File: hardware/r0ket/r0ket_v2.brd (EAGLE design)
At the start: 127.6 x 60.4 mm, 89 parts, among them IC1 MCP1700, IC2 LPC1343, IC3 AT45DB041D, IC4 NRF24L01SMD, IC5 MCP73833, IC6 TB62737, M0DULA M06X2PTH, M0DULB M06X2PTH, Q1 Q12M-SMD-S, Q2 3.2X2.5CRYSTAL, SW1 JS102011SAQN, T1 SI2301DS, T3 SI2301DS, T4 SI2301DS, T5 SI2301DS, T6 SI2301DS, X1 MICROUSB, X1_ JST-PH3, X2 NOKIA

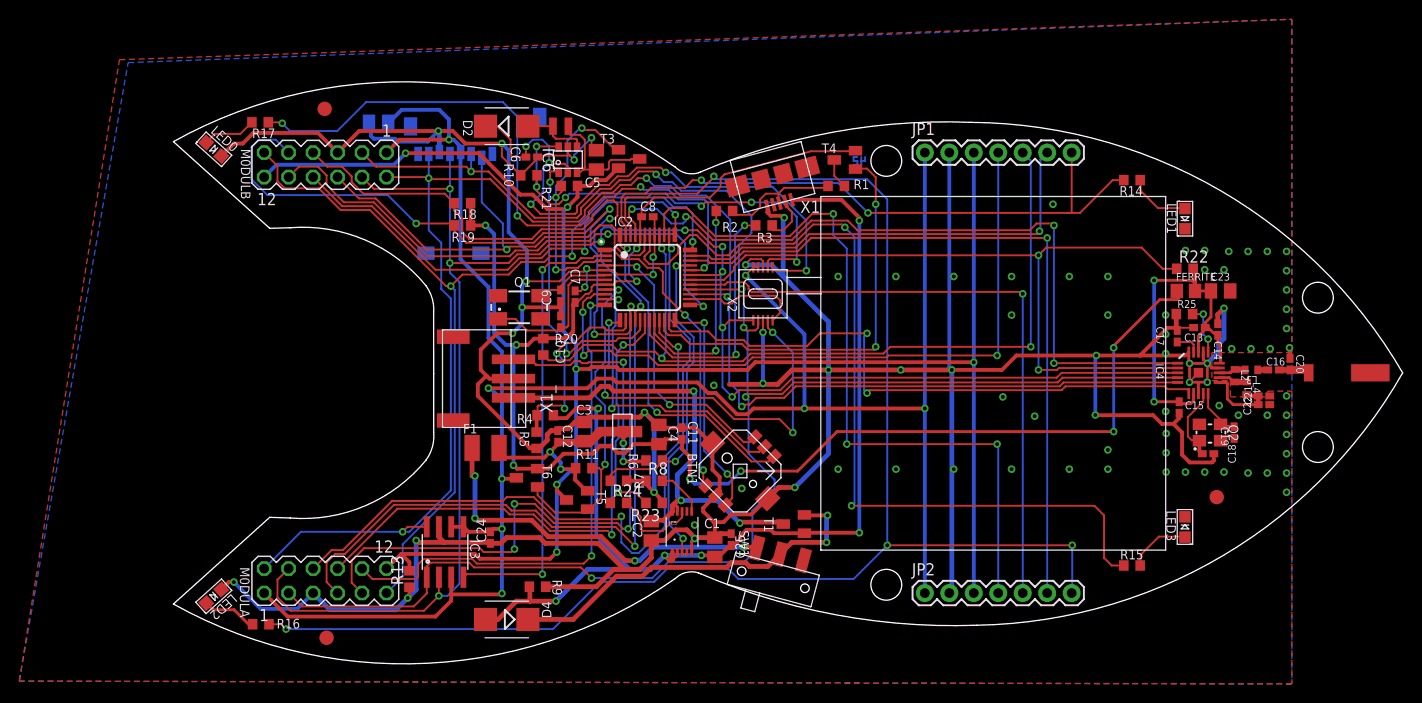
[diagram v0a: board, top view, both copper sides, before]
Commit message: removed a lot of components
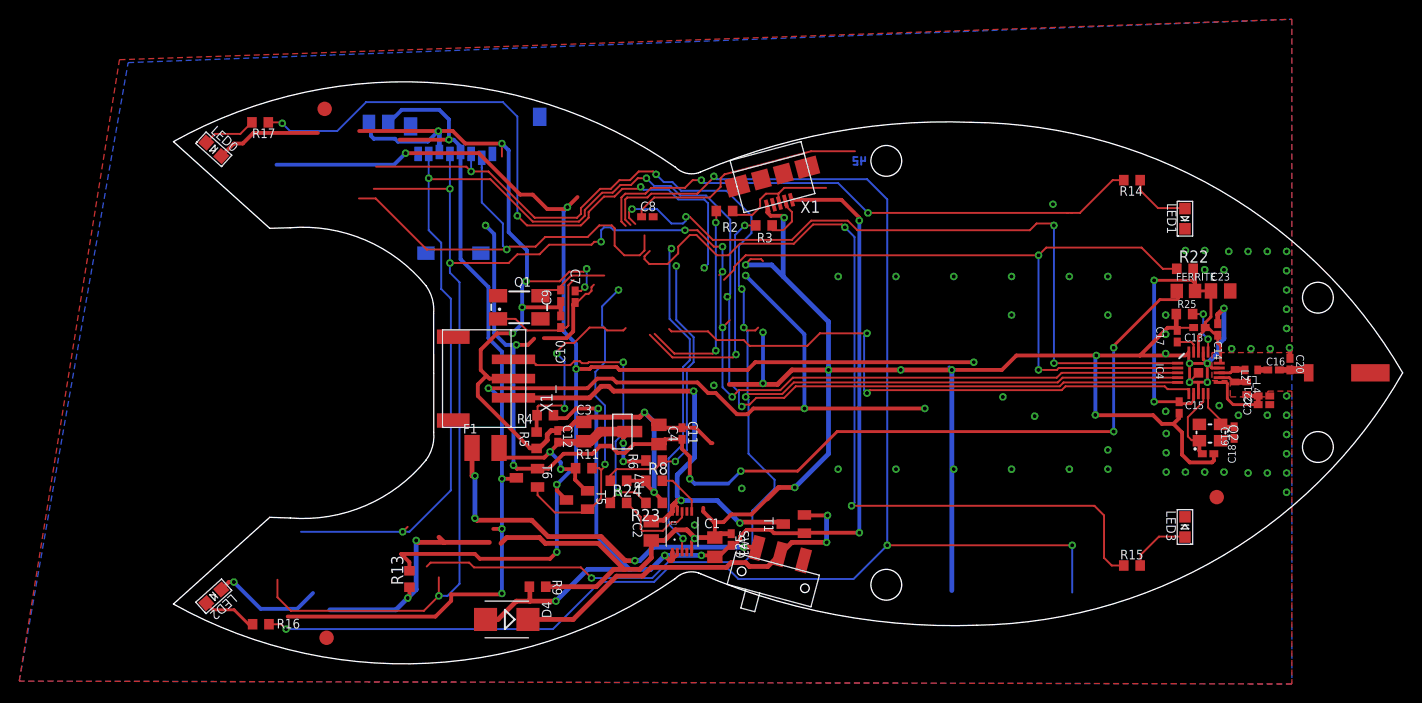
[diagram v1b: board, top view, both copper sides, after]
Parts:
- removed BTN1: MCMT5-F-V, badge:MCMT5-F-V
- removed C24, C6: 100nF, rcl:C0402K
- removed C5: 10uF, rcl:C0805K
- removed D2: SS14, diode:SMB
- removed IC2: LPC1343, microbuilder:LQFP48
- removed IC3: AT45DB041D, SparkFun:SO08
- removed IC6: TB62737, badge:SUPERSOT6
- removed JP1, JP2: (no value), SparkFun:1X07
- removed L1: 4u7, badge:0806
- removed M0DULA, M0DULB: M06X2PTH, con-lstb:MA06-2
- removed R1: 1k5, rcl:R0603
- removed R10: 15, rcl:R0603
- removed R18, R19: 4k7, rcl:R0603
- removed R20: 100k, rcl:R0603
- removed R21: 10k, rcl:R0603
- removed T3, T4: SI2301DS, transistor-small-signal:SOT23
- removed X2: NOKIA, badge:DF23
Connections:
- removed net BTN0: BTN1.3, IC2.4
- removed net BTN1: BTN1.4, IC2.24
- removed net BTN2: BTN1.6, IC2.1
- removed net BTN3: BTN1.1, IC2.48
- removed net BTN4: BTN1.2, IC2.11
- removed net BUSINT: IC2.36, M0DULA.11, M0DULB.11
- removed net CS_DF: IC2.2, IC3.4
- removed net HB0: IC2.39, JP2.4
- removed net HB1: IC2.29, JP2.5
- removed net HB2: IC2.34, JP2.6
- removed net HB3: IC2.10, JP1.4
- removed net HB4: IC2.40, JP1.5, R20.1
- removed net HB5: IC2.35, JP1.6
- removed net LCD_BL: IC2.17, IC6.1
- removed net LCD_BLEN: IC2.3, R21.1, T3.1
- removed net LCD_CS: IC2.13, X2.4
- removed net LCD_RST: IC2.26, X2.5
- removed net LED+: C6.2, D2.C, IC6.2, X2.6
- removed net LED-: IC6.6, R10.2, X2.7
- removed net N$14: D2.A, IC6.4, L1.2
- removed net N$20: R1.1, T4.3
- removed net SCL: IC2.15, M0DULA.9, M0DULB.9, R19.1
- removed net SDA: IC2.16, M0DULA.7, M0DULB.7, R18.2
- removed net SS0: IC2.21, M0DULA.6
- removed net SS1: IC2.18, M0DULA.8
- removed net SS2: IC2.12, M0DULA.10
- removed net SS4: IC2.37, M0DULB.8
- removed net SS5: IC2.25, M0DULB.10
- removed net USB_CONNECT: IC2.22, T4.1
- removed net VCC_LCD: C5.2, IC6.3, L1.1, T3.3
- net +3V3: no longer IC2.44, IC2.8, R18.1, R19.2, R20.2, T4.2
- net +3V3_EXP: no longer C24.2, IC3.3, IC3.5, IC3.6, JP1.1, JP2.1, M0DULA.1, M0DULB.1, X2.10, X2.9
- net CE: no longer IC2.45
- net CHRG_STAT: no longer IC2.38
- net CSN: no longer IC2.30
- net D+: no longer R1.2
- net GND: no longer BTN1.5, BTN1.TAB1, BTN1.TAB2, C24.1, C5.1, C6.1, IC2.41, IC2.5, IC3.7, IC6.5, JP1.2, JP2.2, M0DULA.5, M0DULB.5, R10.1, X2.3, X2.8
- net IRQ: no longer IC2.23
- net LED0: no longer IC2.32
- net LED1: no longer IC2.47, JP1.7
- net LED2: no longer IC2.46, JP2.7
- net LED3: no longer IC2.42
- net MISO: no longer IC2.27, IC3.8, M0DULA.2, M0DULB.2
- net MOSI: no longer IC2.28, IC3.1, M0DULA.3, M0DULB.3, X2.2
- net N$1: no longer IC2.6
- net N$3: no longer IC2.7
- net POWER_GOOD: no longer IC2.9
- net SCK: no longer IC2.31, IC3.2, M0DULA.4, M0DULB.4, X2.1
- net SS3: no longer IC2.43, M0DULB.6
- net USB_DM: no longer IC2.19
- net USB_DP: no longer IC2.20
- net USB_VBUS: no longer IC2.14
- net VCC_EXP: no longer JP1.3, JP2.3, M0DULA.12, M0DULB.12, R21.2, T3.2
- net VOLTAGE: no longer IC2.33
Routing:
- net SCL: track 133.0 -> 0.00 mm, vias 7 -> 0
- net SDA: track 119.8 -> 0.00 mm, vias 3 -> 0
- net BUSINT: track 96.0 -> 0.00 mm, vias 3 -> 0
- net HB4: track 86.8 -> 0.00 mm, vias 3 -> 0
- net HB0: track 77.8 -> 0.00 mm, vias 3 -> 0
- net HB2: track 75.1 -> 0.00 mm, vias 1 -> 0
- net HB3: track 73.4 -> 0.00 mm, vias 3 -> 0
- net GND: track 469.3 -> 397.6 mm, vias 90 -> 86
- net SS0: track 68.1 -> 0.00 mm, vias 2 -> 0
- net HB1: track 66.9 -> 0.00 mm, vias 1 -> 0
- net LED+: track 62.6 -> 0.00 mm, vias 5 -> 0
- net +3V3_EXP: track 215.3 -> 156.1 mm
- net SS1: track 56.6 -> 0.00 mm, vias 2 -> 0
- net SS5: track 56.2 -> 0.00 mm, vias 2 -> 0
- net VCC_EXP: track 190.7 -> 134.8 mm
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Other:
- board text removed: ".badge.events.ccc"
- board text removed: ".de"
- board text removed: "1"
- board text removed: "HB1"
- board text removed: "HB2"
- board text removed: "designed by ccc"
- board text removed: "m0dul A"
- board text removed: "m0dul B"
- board text removed: "r0ket"
